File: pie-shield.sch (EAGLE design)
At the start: 20 parts, among them IC4 NRF24L01SMD, Q2 3.2X2.5CRYSTAL

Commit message: minified and dru tested
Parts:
- added IC1: MAX481CSA, maxim:MAX481CSA
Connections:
- new net N$1: U$1.GND@25
- new net N$2: U$1.GPIO7,SPI0_CE1
- new net N$4: U$1.GPIO8,SPI0_CE0
- new net N$5: U$1.GPIO25
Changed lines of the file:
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@@
 <part name="Q2" library="badge" deviceset="3.2X2.5CRYSTAL" device=""/>
 <part name="ANT" library="badge" deviceset="CHIPANTENNA" device=""/>
+<part name="IC1" library="maxim" deviceset="MAX481CSA" device=""/>
 </parts>
 <sheets>
@@
 <instance part="Q2" gate="G$1" x="248.92" y="78.74"/>
 <instance part="ANT" gate="G$1" x="317.5" y="111.76"/>
+<instance part="IC1" gate="G$1" x="106.68" y="144.78"/>
 </instances>
 <busses>
@@
 </segment>
 </net>
+<net name="N$1" class="0">
+<segment>
+<pinref part="U$1" gate="G$1" pin="GND@25"/>
+<wire x1="60.96" y1="116.84" x2="73.66" y2="116.84" width="0.1524" layer="91"/>
+</segment>
+</net>
+<net name="N$2" class="0">
+<segment>
+<pinref part="U$1" gate="G$1" pin="GPIO7,SPI0_CE1"/>
+<wire x1="5.08" y1="116.84" x2="-2.54" y2="116.84" width="0.1524" layer="91"/>
+</segment>
+</net>
+<net name="N$4" class="0">
+<segment>
+<pinref part="U$1" gate="G$1" pin="GPIO8,SPI0_CE0"/>
+<wire x1="5.08" y1="114.3" x2="-2.54" y2="114.3" width="0.1524" layer="91"/>
+</segment>
+</net>
+<net name="N$5" class="0">
+<segment>
+<pinref part="U$1" gate="G$1" pin="GPIO25"/>
+<wire x1="5.08" y1="111.76" x2="-2.54" y2="111.76" width="0.1524" layer="91"/>
+</segment>
+</net>

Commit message: 1 square inch reached
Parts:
- removed IC1: MAX481CSA, maxim:MAX481CSA
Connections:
- removed net N$2: U$1.GPIO7,SPI0_CE1
- removed net N$5: U$1.GPIO25
- net +3V3: now also U$1.3V3@17; no longer U$1.3V3@1
- net CE: now also U$1.GPIO25
- net CSN: now also U$1.GPIO8,SPI0_CE0
- net GND: now also U$1.GND@25
- net IRQ: now also U$1.GPIO7,SPI0_CE1
- net N$1: now also U$1.GPIO22; no longer U$1.GND@25
- net N$3: now also U$1.GPIO24; no longer U$1.3V3@17
- net N$4: now also U$1.GPIO23; no longer U$1.GPIO8,SPI0_CE0
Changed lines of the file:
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@@
 <part name="Q2" library="badge" deviceset="3.2X2.5CRYSTAL" device=""/>
 <part name="ANT" library="badge" deviceset="CHIPANTENNA" device=""/>
-<part name="IC1" library="maxim" deviceset="MAX481CSA" device=""/>
 </parts>
 <sheets>
@@
 <instance part="Q2" gate="G$1" x="248.92" y="78.74"/>
 <instance part="ANT" gate="G$1" x="317.5" y="111.76"/>
-<instance part="IC1" gate="G$1" x="106.68" y="144.78"/>
 </instances>
 <busses>
@@
 <segment>
 <pinref part="U$1" gate="G$1" pin="GND@20"/>
-<wire x1="5.08" y1="109.22" x2="-5.08" y2="109.22" width="0.1524" layer="91"/>
+<wire x1="5.08" y1="109.22" x2="-10.16" y2="109.22" width="0.1524" layer="91"/>
+<label x="-10.16" y="109.22" size="1.778" layer="95"/>
 </segment>
 <segment>
 <pinref part="U$1" gate="G$1" pin="GND@14"/>
-<wire x1="5.08" y1="101.6" x2="-7.62" y2="101.6" width="0.1524" layer="91"/>
+<wire x1="5.08" y1="101.6" x2="-5.08" y2="101.6" width="0.1524" layer="91"/>
+<wire x1="-5.08" y1="101.6" x2="-7.62" y2="101.6" width="0.1524" layer="91"/>
+<wire x1="-7.62" y1="101.6" x2="-10.16" y2="101.6" width="0.1524" layer="91"/>
+<label x="-10.16" y="101.6" size="1.778" layer="95"/>
 </segment>
 <segment>
 <pinref part="U$1" gate="G$1" pin="GND@9"/>
 <wire x1="60.96" y1="96.52" x2="73.66" y2="96.52" width="0.1524" layer="91"/>
+<label x="73.66" y="96.52" size="1.778" layer="95"/>
+</segment>
+<segment>
+<pinref part="U$1" gate="G$1" pin="GND@25"/>
+<wire x1="60.96" y1="116.84" x2="73.66" y2="116.84" width="0.1524" layer="91"/>
+<label x="73.66" y="116.84" size="1.778" layer="95"/>
 </segment>
 </net>
@@
 </segment>
 <segment>
-<pinref part="U$1" gate="G$1" pin="3V3@1"/>
-<wire x1="60.96" y1="86.36" x2="71.12" y2="86.36" width="0.1524" layer="91"/>
+<pinref part="U$1" gate="G$1" pin="3V3@17"/>
+<wire x1="60.96" y1="106.68" x2="73.66" y2="106.68" width="0.1524" layer="91"/>
+<label x="73.66" y="106.68" size="1.778" layer="95"/>
 </segment>
 </net>
@@
 <pinref part="U$1" gate="G$1" pin="GPIO9_MISO"/>
 <wire x1="60.96" y1="111.76" x2="73.66" y2="111.76" width="0.1524" layer="91"/>
+<label x="73.66" y="111.76" size="1.778" layer="95"/>
 </segment>
 </net>
@@
 <pinref part="U$1" gate="G$1" pin="GPIO10_MOSI"/>
 <wire x1="73.66" y1="109.22" x2="60.96" y2="109.22" width="0.1524" layer="91"/>
+<label x="73.66" y="109.22" size="1.778" layer="95"/>
 </segment>
 </net>
@@
 <pinref part="U$1" gate="G$1" pin="GPIO11_SCLK"/>
 <wire x1="60.96" y1="114.3" x2="73.66" y2="114.3" width="0.1524" layer="91"/>
+<label x="73.66" y="114.3" size="1.778" layer="95"/>
 </segment>
 </net>
@@
 <pinref part="IC4" gate="G$1" pin="CE"/>
 </segment>
+<segment>
+<pinref part="U$1" gate="G$1" pin="GPIO25"/>
+<wire x1="5.08" y1="111.76" x2="-10.16" y2="111.76" width="0.1524" layer="91"/>
+<label x="-10.16" y="111.76" size="1.778" layer="95"/>
+</segment>
 </net>
 <net name="CSN" class="0">
@@
 <label x="193.04" y="111.76" size="1.778" layer="95"/>
 <pinref part="IC4" gate="G$1" pin="CSN"/>
+</segment>
+<segment>
+<pinref part="U$1" gate="G$1" pin="GPIO8,SPI0_CE0"/>
+<wire x1="5.08" y1="114.3" x2="-10.16" y2="114.3" width="0.1524" layer="91"/>
+<label x="-10.16" y="114.3" size="1.778" layer="95"/>
 </segment>
 </net>
@@
 <pinref part="IC4" gate="G$1" pin="IRQ"/>
 </segment>
+<segment>
+<pinref part="U$1" gate="G$1" pin="GPIO7,SPI0_CE1"/>
+<wire x1="5.08" y1="116.84" x2="-2.54" y2="116.84" width="0.1524" layer="91"/>
+<label x="-2.54" y="116.84" size="1.778" layer="95"/>
+<label x="-2.54" y="116.84" size="1.778" layer="95"/>
+</segment>
 </net>
 <net name="N$10" class="0">
@@
 </segment>
 </net>
+<net name="N$1" class="0">
+<segment>
+<pinref part="U$1" gate="G$1" pin="GPIO22"/>
+<wire x1="60.96" y1="104.14" x2="73.66" y2="104.14" width="0.1524" layer="91"/>
+</segment>
+</net>
 <net name="N$3" class="0">
 <segment>
-<pinref part="U$1" gate="G$1" pin="3V3@17"/>
-<wire x1="60.96" y1="106.68" x2="73.66" y2="106.68" width="0.1524" layer="91"/>
-</segment>
-</net>
-<net name="N$1" class="0">
-<segment>
-<pinref part="U$1" gate="G$1" pin="GND@25"/>
-<wire x1="60.96" y1="116.84" x2="73.66" y2="116.84" width="0.1524" layer="91"/>
-</segment>
-</net>
-<net name="N$2" class="0">
-<segment>
-<pinref part="U$1" gate="G$1" pin="GPIO7,SPI0_CE1"/>
-<wire x1="5.08" y1="116.84" x2="-2.54" y2="116.84" width="0.1524" layer="91"/>
+<pinref part="U$1" gate="G$1" pin="GPIO24"/>
+<wire x1="5.08" y1="106.68" x2="-10.16" y2="106.68" width="0.1524" layer="91"/>
 </segment>
 </net>
 <net name="N$4" class="0">
 <segment>
-<pinref part="U$1" gate="G$1" pin="GPIO8,SPI0_CE0"/>
-<wire x1="5.08" y1="114.3" x2="-2.54" y2="114.3" width="0.1524" layer="91"/>
-</segment>
-</net>
-<net name="N$5" class="0">
-<segment>
-<pinref part="U$1" gate="G$1" pin="GPIO25"/>
-<wire x1="5.08" y1="111.76" x2="-2.54" y2="111.76" width="0.1524" layer="91"/>
-</segment>
-</net>
+<pinref part="U$1" gate="G$1" pin="GPIO23"/>
+<wire x1="5.08" y1="104.14" x2="-7.62" y2="104.14" width="0.1524" layer="91"/>
+</segment>
+</net>

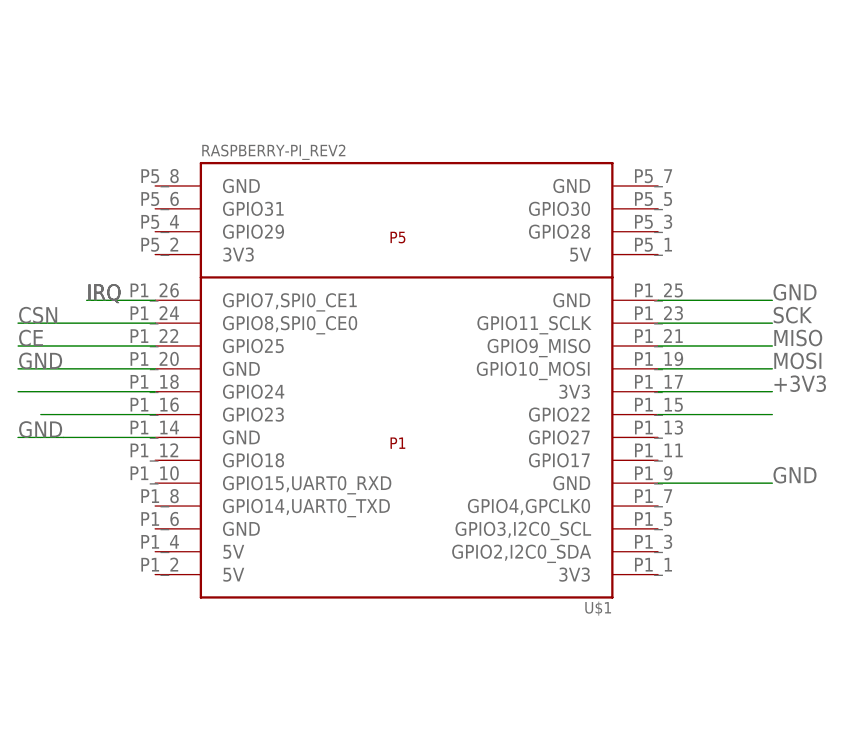
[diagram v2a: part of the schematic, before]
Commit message: updated to smaller version of raspberry io
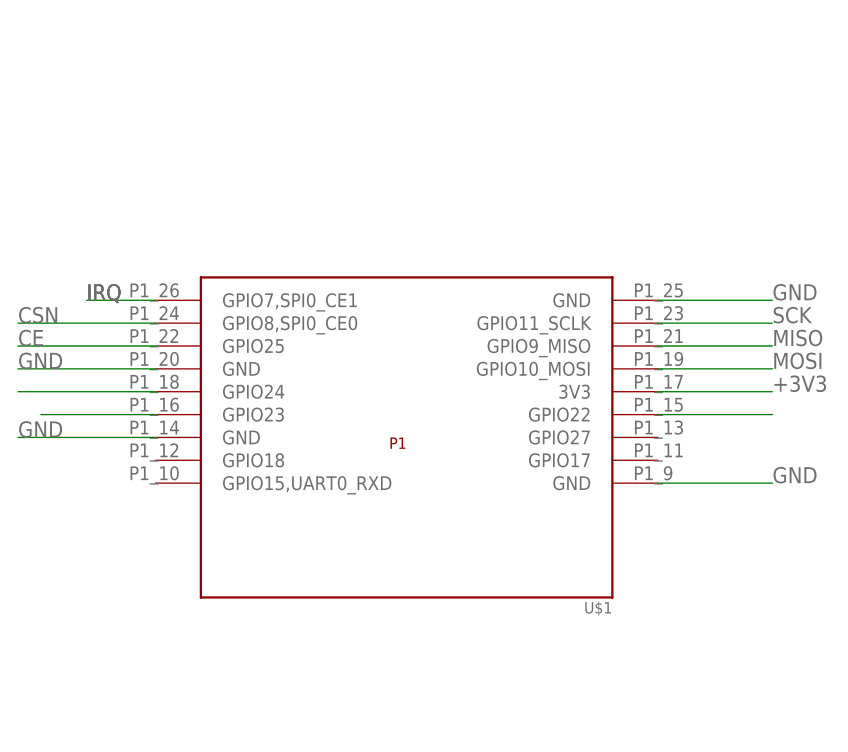
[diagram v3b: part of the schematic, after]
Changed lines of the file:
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@@
 <grid distance="0.1" unitdist="inch" unit="inch" style="lines" multiple="1" display="no" altdistance="0.01" altunitdist="inch" altunit="inch"/>
 <layers>
-<layer number="1" name="Top" color="4" fill="1" visible="no" active="no"/>
-<layer number="2" name="Route2" color="1" fill="3" visible="no" active="no"/>
-<layer number="3" name="Route3" color="4" fill="3" visible="no" active="no"/>
-<layer number="4" name="Route4" color="1" fill="4" visible="no" active="no"/>
-<layer number="5" name="Route5" color="4" fill="4" visible="no" active="no"/>
-<layer number="6" name="Route6" color="1" fill="8" visible="no" active="no"/>
-<layer number="7" name="Route7" color="4" fill="8" visible="no" active="no"/>
-<layer number="8" name="Route8" color="1" fill="2" visible="no" active="no"/>
-<layer number="9" name="Route9" color="4" fill="2" visible="no" active="no"/>
-<layer number="10" name="Route10" color="1" fill="7" visible="no" active="no"/>
-<layer number="11" name="Route11" color="4" fill="7" visible="no" active="no"/>
-<layer number="12" name="Route12" color="1" fill="5" visible="no" active="no"/>
-<layer number="13" name="Route13" color="4" fill="5" visible="no" active="no"/>
-<layer number="14" name="Route14" color="1" fill="6" visible="no" active="no"/>
-<layer number="15" name="Route15" color="4" fill="6" visible="no" active="no"/>
-<layer number="16" name="Bottom" color="1" fill="1" visible="no" active="no"/>
-<layer number="17" name="Pads" color="2" fill="1" visible="no" active="no"/>
-<layer number="18" name="Vias" color="2" fill="1" visible="no" active="no"/>
-<layer number="19" name="Unrouted" color="6" fill="1" visible="no" active="no"/>
-<layer number="20" name="Dimension" color="15" fill="1" visible="no" active="no"/>
-<layer number="21" name="tPlace" color="7" fill="1" visible="no" active="no"/>
-<layer number="22" name="bPlace" color="7" fill="1" visible="no" active="no"/>
-<layer number="23" name="tOrigins" color="15" fill="1" visible="no" active="no"/>
-<layer number="24" name="bOrigins" color="15" fill="1" visible="no" active="no"/>
-<layer number="25" name="tNames" color="7" fill="1" visible="no" active="no"/>
-<layer number="26" name="bNames" color="7" fill="1" visible="no" active="no"/>
-<layer number="27" name="tValues" color="7" fill="1" visible="no" active="no"/>
-<layer number="28" name="bValues" color="7" fill="1" visible="no" active="no"/>
+<layer number="1" name="Top" color="4" fill="1" visible="yes" active="no"/>
+<layer number="2" name="Route2" color="1" fill="3" visible="yes" active="no"/>
+<layer number="3" name="Route3" color="4" fill="3" visible="yes" active="no"/>
+<layer number="4" name="Route4" color="1" fill="4" visible="yes" active="no"/>
+<layer number="5" name="Route5" color="4" fill="4" visible="yes" active="no"/>
+<layer number="6" name="Route6" color="1" fill="8" visible="yes" active="no"/>
+<layer number="7" name="Route7" color="4" fill="8" visible="yes" active="no"/>
+<layer number="8" name="Route8" color="1" fill="2" visible="yes" active="no"/>
+<layer number="9" name="Route9" color="4" fill="2" visible="yes" active="no"/>
+<layer number="10" name="Route10" color="1" fill="7" visible="yes" active="no"/>
+<layer number="11" name="Route11" color="4" fill="7" visible="yes" active="no"/>
+<layer number="12" name="Route12" color="1" fill="5" visible="yes" active="no"/>
+<layer number="13" name="Route13" color="4" fill="5" visible="yes" active="no"/>
+<layer number="14" name="Route14" color="1" fill="6" visible="yes" active="no"/>
+<layer number="15" name="Route15" color="4" fill="6" visible="yes" active="no"/>
+<layer number="16" name="Bottom" color="1" fill="1" visible="yes" active="no"/>
+<layer number="17" name="Pads" color="2" fill="1" visible="yes" active="no"/>
+<layer number="18" name="Vias" color="2" fill="1" visible="yes" active="no"/>
+<layer number="19" name="Unrouted" color="6" fill="1" visible="yes" active="no"/>
+<layer number="20" name="Dimension" color="15" fill="1" visible="yes" active="no"/>
+<layer number="21" name="tPlace" color="7" fill="1" visible="yes" active="no"/>
+<layer number="22" name="bPlace" color="7" fill="1" visible="yes" active="no"/>
+<layer number="23" name="tOrigins" color="15" fill="1" visible="yes" active="no"/>
+<layer number="24" name="bOrigins" color="15" fill="1" visible="yes" active="no"/>
+<layer number="25" name="tNames" color="7" fill="1" visible="yes" active="no"/>
+<layer number="26" name="bNames" color="7" fill="1" visible="yes" active="no"/>
+<layer number="27" name="tValues" color="7" fill="1" visible="yes" active="no"/>
+<layer number="28" name="bValues" color="7" fill="1" visible="yes" active="no"/>
 <layer number="29" name="tStop" color="7" fill="3" visible="no" active="no"/>
 <layer number="30" name="bStop" color="7" fill="6" visible="no" active="no"/>
@@
 <layer number="35" name="tGlue" color="7" fill="4" visible="no" active="no"/>
 <layer number="36" name="bGlue" color="7" fill="5" visible="no" active="no"/>
-<layer number="37" name="tTest" color="7" fill="1" visible="no" active="no"/>
-<layer number="38" name="bTest" color="7" fill="1" visible="no" active="no"/>
+<layer number="37" name="tTest" color="7" fill="1" visible="yes" active="no"/>
+<layer number="38" name="bTest" color="7" fill="1" visible="yes" active="no"/>
 <layer number="39" name="tKeepout" color="4" fill="11" visible="no" active="no"/>
 <layer number="40" name="bKeepout" color="1" fill="11" visible="no" active="no"/>
@@
 <layer number="44" name="Drills" color="7" fill="1" visible="no" active="no"/>
 <layer number="45" name="Holes" color="7" fill="1" visible="no" active="no"/>
-<layer number="46" name="Milling" color="3" fill="1" visible="no" active="no"/>
-<layer number="47" name="Measures" color="7" fill="1" visible="no" active="no"/>
-<layer number="48" name="Document" color="7" fill="1" visible="no" active="no"/>
-<layer number="49" name="Reference" color="7" fill="1" visible="no" active="no"/>
-<layer number="50" name="dxf" color="7" fill="1" visible="no" active="no"/>
-<layer number="51" name="tDocu" color="14" fill="1" visible="no" active="no"/>
-<layer number="52" name="bDocu" color="7" fill="1" visible="no" active="no"/>
-<layer number="53" name="tGND_GNDA" color="7" fill="9" visible="no" active="no"/>
-<layer number="54" name="bGND_GNDA" color="1" fill="9" visible="no" active="no"/>
-<layer number="56" name="wert" color="7" fill="1" visible="no" active="no"/>
+<layer number="46" name="Milling" color="3" fill="1" visible="yes" active="no"/>
+<layer number="47" name="Measures" color="7" fill="1" visible="yes" active="no"/>
+<layer number="48" name="Document" color="7" fill="1" visible="yes" active="no"/>
+<layer number="49" name="Reference" color="7" fill="1" visible="yes" active="no"/>
+<layer number="50" name="dxf" color="7" fill="1" visible="yes" active="no"/>
+<layer number="51" name="tDocu" color="14" fill="1" visible="yes" active="no"/>
+<layer number="52" name="bDocu" color="7" fill="1" visible="yes" active="no"/>
+<layer number="53" name="tGND_GNDA" color="7" fill="9" visible="yes" active="no"/>
+<layer number="54" name="bGND_GNDA" color="1" fill="9" visible="yes" active="no"/>
+<layer number="56" name="wert" color="7" fill="1" visible="yes" active="no"/>
 <layer number="91" name="Nets" color="2" fill="1" visible="yes" active="yes"/>
 <layer number="92" name="Busses" color="1" fill="1" visible="yes" active="yes"/>

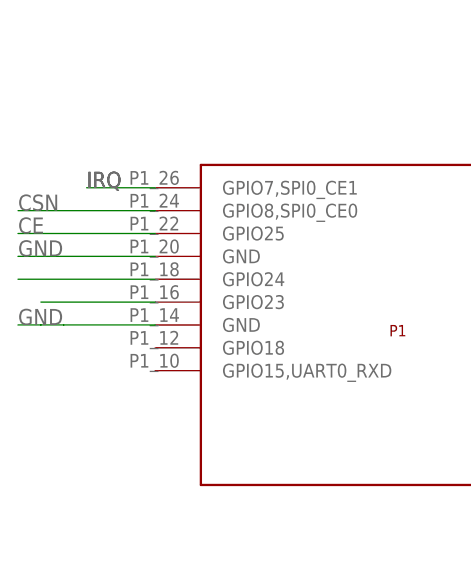
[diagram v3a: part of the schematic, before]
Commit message: fixed drill holes - removed
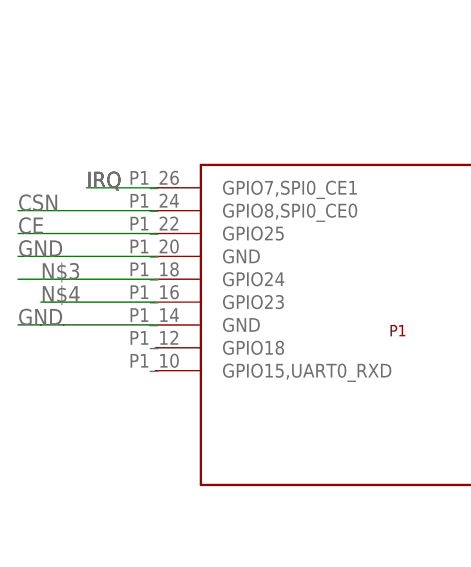
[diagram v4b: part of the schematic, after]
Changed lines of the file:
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@@
 <pinref part="U$1" gate="G$1" pin="GPIO24"/>
 <wire x1="5.08" y1="106.68" x2="-10.16" y2="106.68" width="0.1524" layer="91"/>
+<label x="-7.62" y="106.68" size="1.778" layer="95"/>
 </segment>
 </net>
@@
 <pinref part="U$1" gate="G$1" pin="GPIO23"/>
 <wire x1="5.08" y1="104.14" x2="-7.62" y2="104.14" width="0.1524" layer="91"/>
+<label x="-7.62" y="104.14" size="1.778" layer="95"/>
 </segment>
 </net>
